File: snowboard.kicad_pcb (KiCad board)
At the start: 4 copper layers, 80 x 104.5 mm, 6 parts, among them J1 AMPHENOL_10118193-0001LF, SW1 BOOT, SW2 RESET, U1 XCVR_ESP32-WROVER-E-N4R8, U2 IC_CP2102N-A02-GQFN28R

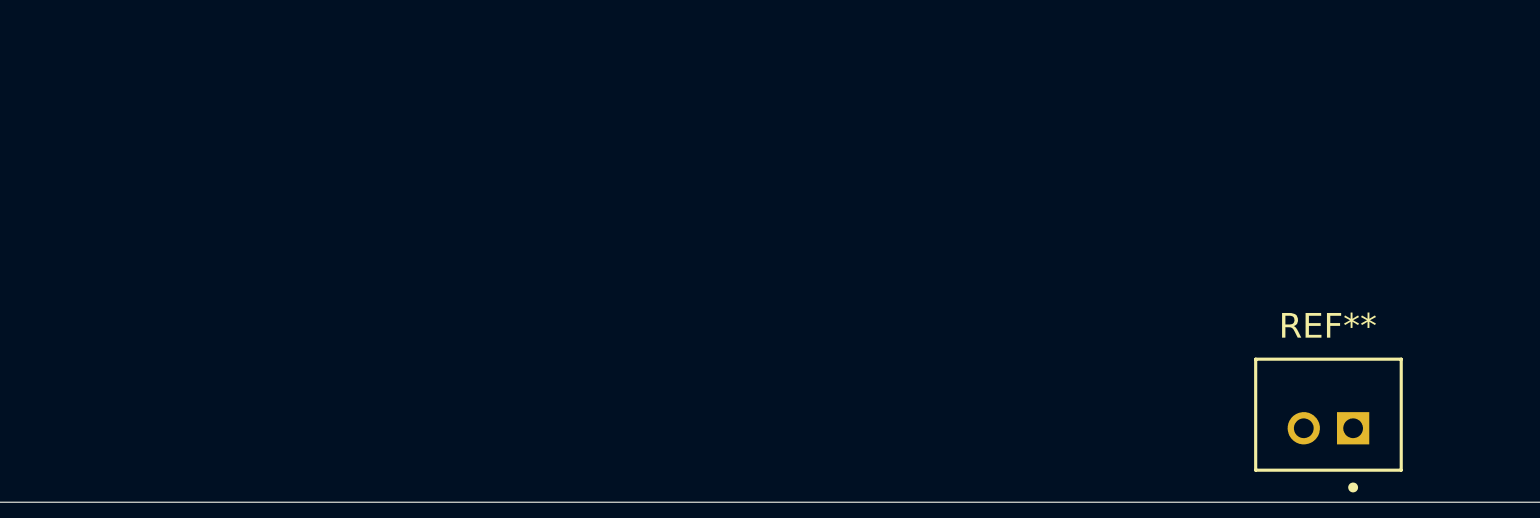
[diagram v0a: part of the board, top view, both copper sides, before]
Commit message: Update battery connector
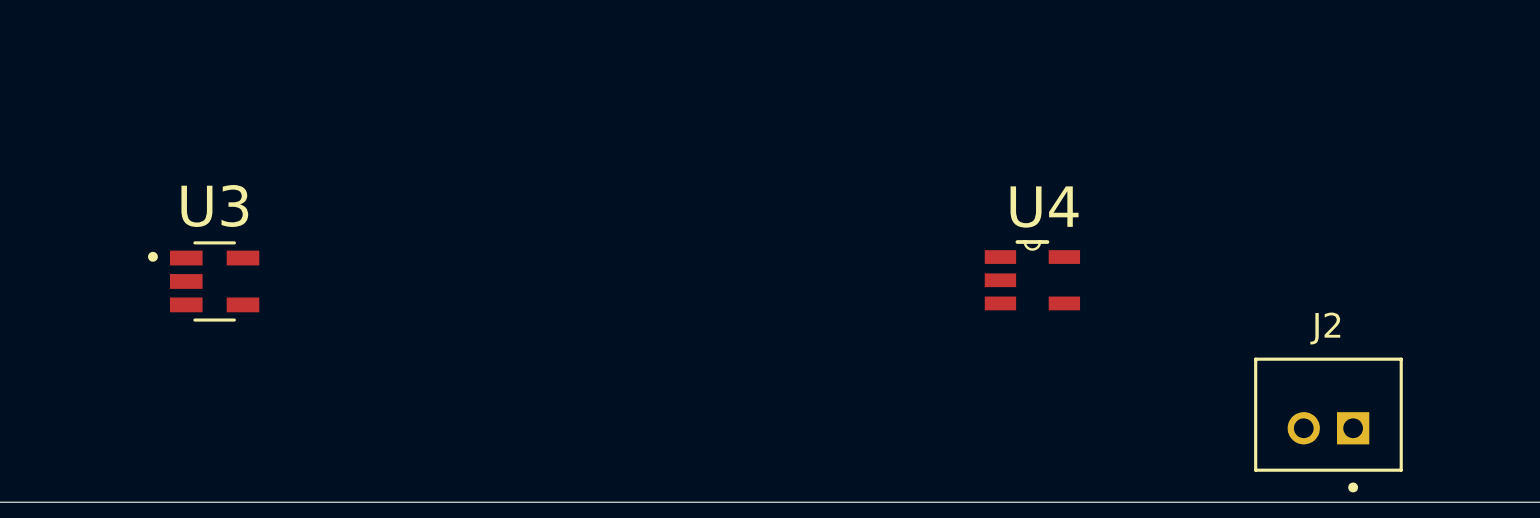
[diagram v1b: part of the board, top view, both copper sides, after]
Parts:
- added U3: SOT95P280X145-5N, USER_FP:SOT95P280X145-5N, F.Cu at (127.8, 146.1)
- added U4: SOT95P280X145-5N, USER_FP:MCP73831T-2ACI, F.Cu at (161.0, 146.0)
- renumbered REF** to J2

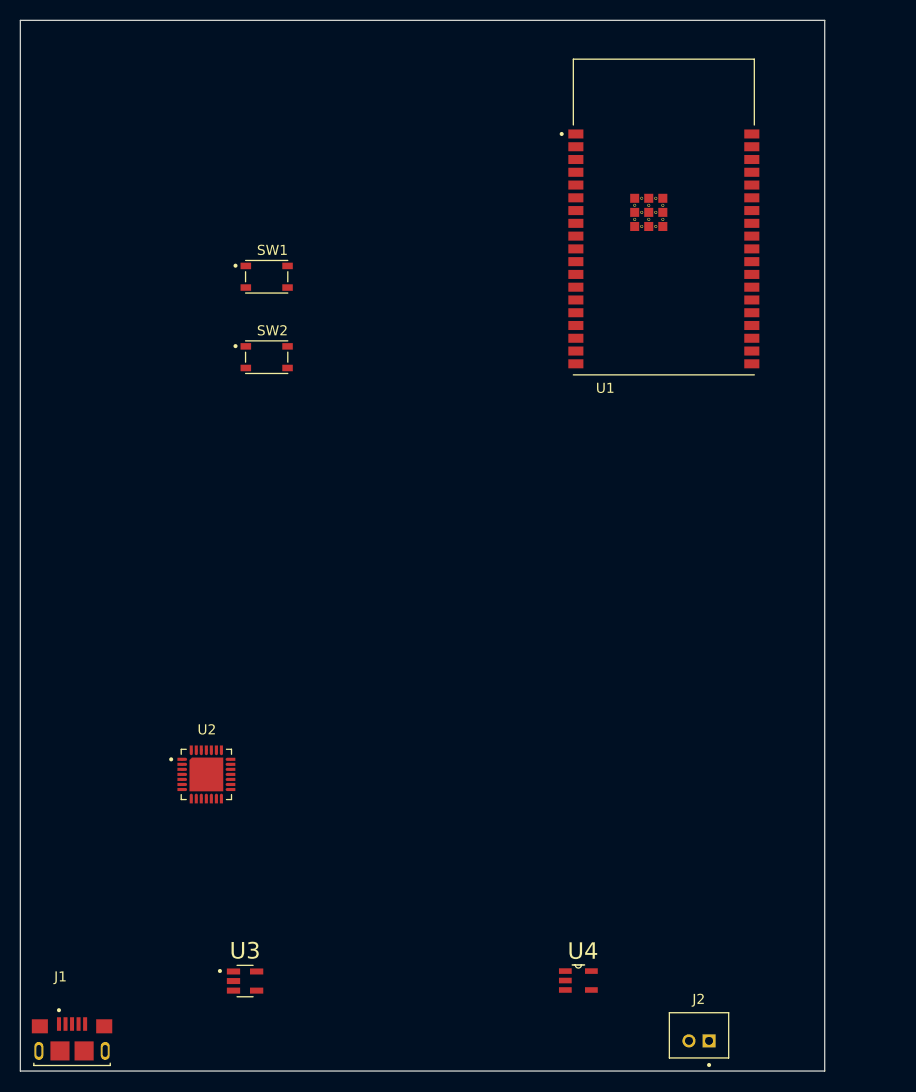
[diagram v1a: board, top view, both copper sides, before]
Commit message: Add footprints and models and place components on PCB
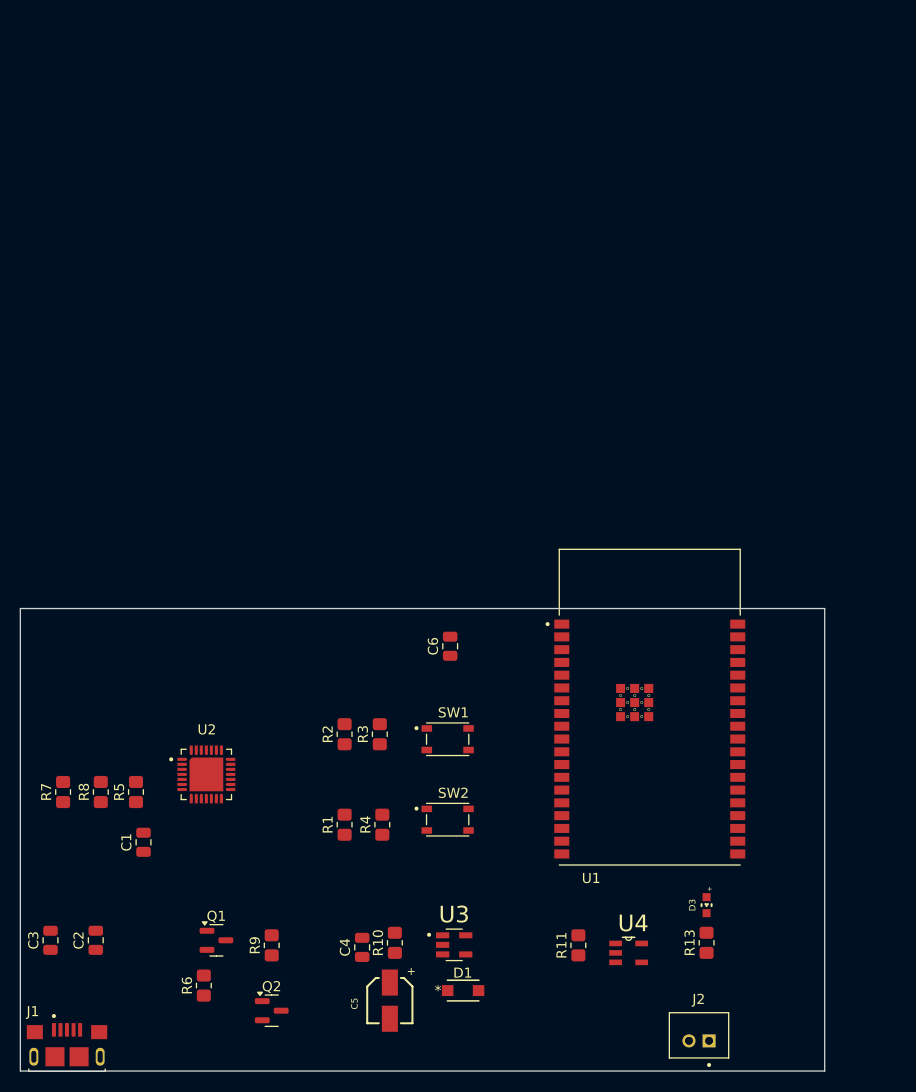
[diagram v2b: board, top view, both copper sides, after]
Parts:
- added C1: 1uF, Capacitor_SMD:C_0805_2012Metric, F.Cu at (117.8, 132.2)
- added C2: 10uF, Capacitor_SMD:C_0805_2012Metric, F.Cu at (113.0, 142.0)
- added C3: 100nF, Capacitor_SMD:C_0805_2012Metric, F.Cu at (108.5, 142.0)
- added C4: 10uF, Capacitor_SMD:C_0805_2012Metric, F.Cu at (139.5, 142.7)
- added C5: 1uF, USER_FP:WCAP-ASLL_4X5.5_DXL_, F.Cu at (142.2, 148.0)
- added C6: 10uF, Capacitor_SMD:C_0805_2012Metric, F.Cu at (148.2, 112.8)
- added D1: MBR120, USER_FP:MBR120_SDO_SOD-123FL498_OSI, F.Cu at (149.5, 147.0)
- added D3: Charge Status, USER_FP:WL-SMCW_0603, F.Cu at (173.8, 138.5)
- added Q1: S8050, Package_TO_SOT_SMD:SOT-23, F.Cu at (125.0, 142.0)
- added Q2: S8050, Package_TO_SOT_SMD:SOT-23, F.Cu at (130.5, 149.0)
- added R1: 10k, Resistor_SMD:R_0805_2012Metric_Pad1.20x1.40mm_HandSolder, F.Cu at (137.8, 130.5)
- added R10: 100K, Resistor_SMD:R_0805_2012Metric_Pad1.20x1.40mm_HandSolder, F.Cu at (142.8, 142.2)
- added R11: 5k, Resistor_SMD:R_0805_2012Metric_Pad1.20x1.40mm_HandSolder, F.Cu at (161.0, 142.5)
- added R13: 1k, Resistor_SMD:R_0805_2012Metric_Pad1.20x1.40mm_HandSolder, F.Cu at (173.8, 142.2)
- added R2: 10k, Resistor_SMD:R_0805_2012Metric_Pad1.20x1.40mm_HandSolder, F.Cu at (137.8, 121.5)
- added R3: 470, Resistor_SMD:R_0805_2012Metric_Pad1.20x1.40mm_HandSolder, F.Cu at (141.2, 121.5)
- added R4: 470, Resistor_SMD:R_0805_2012Metric_Pad1.20x1.40mm_HandSolder, F.Cu at (141.5, 130.5)
- added R5: 470, Resistor_SMD:R_0805_2012Metric_Pad1.20x1.40mm_HandSolder, F.Cu at (117.0, 127.2)
- added R6: 12k, Resistor_SMD:R_0805_2012Metric_Pad1.20x1.40mm_HandSolder, F.Cu at (123.8, 146.5)
- added R7: 47.5K, Resistor_SMD:R_0805_2012Metric_Pad1.20x1.40mm_HandSolder, F.Cu at (109.8, 127.2)
- added R8: 22.1K, Resistor_SMD:R_0805_2012Metric_Pad1.20x1.40mm_HandSolder, F.Cu at (113.5, 127.2)
- added R9: 12k, Resistor_SMD:R_0805_2012Metric_Pad1.20x1.40mm_HandSolder, F.Cu at (130.5, 142.5)
- J1: value AMPHENOL_10118193-0001LF -> Micro USB Port
- J2: value JST_B2B-PH-K-S -> B2B-PH-K-S
- U1: value XCVR_ESP32-WROVER-E-N4R8 -> ESP32-WROVER-E-N4R8
- U2: value IC_CP2102N-A02-GQFN28R -> CP2102N-A02-GQFN28R
- U3: value SOT95P280X145-5N -> SPX3819M5-L-3-3
- U4: value SOT95P280X145-5N -> MCP73831T-2ACI_OT
- moved SW1 49.4 mm to (148.0, 122.0)
- moved SW2 49.4 mm to (148.0, 130.0)
- moved U1 48.8 mm to (168.1, 118.8)
- moved U3 21.1 mm to (148.7, 142.4)
- moved U4 5.71 mm to (166.0, 143.2)
- moved J1 0.77 mm to (110.1, 153.6)
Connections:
- J1 pad 1: (no net) -> VBUS
- J1 pad 2: (no net) -> /D_N
- J1 pad 3: (no net) -> /D_P
- J1 pad 4: (no net) -> unconnected-(J1-ID-Pad4)
- J1 pad 5: (no net) -> GND
- J1 pad S1: (no net) -> unconnected-(J1-SHIELD-PadS1)
- J1 pad S2: (no net) -> unconnected-(J1-SHIELD__1-PadS2)
- J1 pad S3: (no net) -> unconnected-(J1-SHIELD__2-PadS3)
- J1 pad S4: (no net) -> unconnected-(J1-SHIELD__3-PadS4)
- J1 pad S5: (no net) -> unconnected-(J1-SHIELD__4-PadS5)
- J1 pad S6: (no net) -> unconnected-(J1-SHIELD__5-PadS6)
- J2 pad 1: (no net) -> +BATT
- J2 pad 2: (no net) -> GND
- SW1 pad 1: (no net) -> Net-(R3-Pad1)
- SW1 pad 2: (no net) -> unconnected-(SW1-Pad2)
- SW1 pad 3: (no net) -> unconnected-(SW1-Pad3)
- SW1 pad 4: (no net) -> /IO0
- SW2 pad 1: (no net) -> Net-(R4-Pad1)
- SW2 pad 2: (no net) -> unconnected-(SW2-Pad2)
- SW2 pad 3: (no net) -> unconnected-(SW2-Pad3)
- SW2 pad 4: (no net) -> /AEN
- U1 pad 1: (no net) -> GND
- U1 pad 10: (no net) -> unconnected-(U1-IO25-Pad10)
- U1 pad 11: (no net) -> unconnected-(U1-IO26-Pad11)
- U1 pad 12: (no net) -> unconnected-(U1-IO27-Pad12)
- U1 pad 13: (no net) -> unconnected-(U1-IO14-Pad13)
- U1 pad 14: (no net) -> unconnected-(U1-IO12-Pad14)
- U1 pad 15: (no net) -> GND
- U1 pad 16: (no net) -> unconnected-(U1-IO13-Pad16)
- U1 pad 17: (no net) -> unconnected-(U1-NC-Pad17)
- U1 pad 18: (no net) -> unconnected-(U1-NC__1-Pad18)
- U1 pad 19: (no net) -> unconnected-(U1-NC__2-Pad19)
- U1 pad 2: (no net) -> +3.3V
- U1 pad 20: (no net) -> unconnected-(U1-NC__3-Pad20)
- U1 pad 21: (no net) -> unconnected-(U1-NC__4-Pad21)
- U1 pad 22: (no net) -> unconnected-(U1-NC__5-Pad22)
- U1 pad 23: (no net) -> unconnected-(U1-IO15-Pad23)
- U1 pad 24: (no net) -> unconnected-(U1-IO2-Pad24)
- U1 pad 25: (no net) -> /IO0
- U1 pad 26: (no net) -> unconnected-(U1-IO4-Pad26)
- U1 pad 27: (no net) -> unconnected-(U1-NC__6-Pad27)
- U1 pad 28: (no net) -> unconnected-(U1-NC__7-Pad28)
- U1 pad 29: (no net) -> unconnected-(U1-IO5-Pad29)
- U1 pad 3: (no net) -> /AEN
- U1 pad 30: (no net) -> unconnected-(U1-IO18-Pad30)
- U1 pad 31: (no net) -> unconnected-(U1-IO19-Pad31)
- U1 pad 32: (no net) -> unconnected-(U1-NC__8-Pad32)
- U1 pad 33: (no net) -> unconnected-(U1-IO21-Pad33)
- U1 pad 34: (no net) -> /RX
- U1 pad 35: (no net) -> /TX
- U1 pad 36: (no net) -> unconnected-(U1-IO22-Pad36)
- U1 pad 37: (no net) -> unconnected-(U1-IO23-Pad37)
- U1 pad 38: (no net) -> GND
- U1 pad 39_1: (no net) -> unconnected-(U1-EXP-Pad39_1)
- U1 pad 39_2: (no net) -> unconnected-(U1-EXP__1-Pad39_2)
- U1 pad 39_3: (no net) -> unconnected-(U1-EXP__2-Pad39_3)
- U1 pad 39_4: (no net) -> unconnected-(U1-EXP__3-Pad39_4)
- U1 pad 39_5: (no net) -> unconnected-(U1-EXP__4-Pad39_5)
- U1 pad 39_6: (no net) -> unconnected-(U1-EXP__5-Pad39_6)
- U1 pad 39_7: (no net) -> unconnected-(U1-EXP__6-Pad39_7)
- U1 pad 39_8: (no net) -> unconnected-(U1-EXP__7-Pad39_8)
- U1 pad 39_9: (no net) -> unconnected-(U1-EXP__8-Pad39_9)
- U1 pad 4: (no net) -> unconnected-(U1-SENSOR_VP-Pad4)
- U1 pad 5: (no net) -> unconnected-(U1-SENSOR_VN-Pad5)
- U1 pad 6: (no net) -> unconnected-(U1-IO34-Pad6)
- U1 pad 7: (no net) -> unconnected-(U1-IO35-Pad7)
- U1 pad 8: (no net) -> unconnected-(U1-IO32-Pad8)
- U1 pad 9: (no net) -> unconnected-(U1-IO33-Pad9)
- U2 pad 1: (no net) -> unconnected-(U2-DCD-Pad1)
- U2 pad 10: (no net) -> unconnected-(U2-NC-Pad10)
- U2 pad 11: (no net) -> unconnected-(U2-~{SUSPEND}-Pad11)
- U2 pad 12: (no net) -> unconnected-(U2-SUSPEND-Pad12)
- U2 pad 13: (no net) -> unconnected-(U2-CHREN-Pad13)
- U2 pad 14: (no net) -> unconnected-(U2-CHR1-Pad14)
- U2 pad 15: (no net) -> unconnected-(U2-CHR0-Pad15)
- U2 pad 16: (no net) -> unconnected-(U2-GPIO3_WAKEUP-Pad16)
- U2 pad 17: (no net) -> unconnected-(U2-GPIO2_RS485-Pad17)
- U2 pad 18: (no net) -> unconnected-(U2-GPIO1_RXT-Pad18)
- U2 pad 19: (no net) -> unconnected-(U2-GPIO0_TXT-Pad19)
- U2 pad 2: (no net) -> unconnected-(U2-RI/CLK-Pad2)
- U2 pad 20: (no net) -> unconnected-(U2-GPIO6-Pad20)
- U2 pad 21: (no net) -> unconnected-(U2-GPIO5-Pad21)
- U2 pad 22: (no net) -> unconnected-(U2-GPIO4-Pad22)
- U2 pad 23: (no net) -> unconnected-(U2-CTS-Pad23)
- U2 pad 24: (no net) -> /RTS
- U2 pad 25: (no net) -> /TX
- U2 pad 26: (no net) -> Net-(U2-TXD)
- U2 pad 27: (no net) -> unconnected-(U2-DSR-Pad27)
- U2 pad 28: (no net) -> /DTR
- U2 pad 29: (no net) -> GND
- U2 pad 3: (no net) -> GND
- U2 pad 4: (no net) -> /D_P
- U2 pad 5: (no net) -> /D_N
- U2 pad 6: (no net) -> Net-(U2-VDD)
- U2 pad 7: (no net) -> VBUS
- U2 pad 8: (no net) -> Net-(U2-VBUS)
- U2 pad 9: (no net) -> unconnected-(U2-~{RST}-Pad9)
- U3 pad 1: (no net) -> VBUS
- U3 pad 2: (no net) -> GND
- U3 pad 3: (no net) -> Net-(U3-EN)
- U3 pad 4: (no net) -> GND
- U3 pad 5: (no net) -> +3.3V
- U4 pad 1: (no net) -> Net-(U4-STAT)
- U4 pad 2: (no net) -> GND
- U4 pad 3: (no net) -> +BATT
- U4 pad 4: (no net) -> VBUS
- U4 pad 5: (no net) -> Net-(U4-PROG)
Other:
- board size 80 x 104.5 mm -> 80 x 46 mm

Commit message: PCB routing mostly done
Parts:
- moved J1 78.6 mm to (184.2, 127.2), turned to 90 degrees
- moved R7 74.5 mm to (183.8, 118.5), turned to -90 degrees
- moved C3 69.2 mm to (175.8, 125.8)
- moved R8 68.8 mm to (181.8, 118.5)
- moved C1 65.9 mm to (182.8, 121.5), turned to 0 degrees
- moved C2 62.9 mm to (173.8, 125.8)
- moved R6 56.1 mm to (168.0, 112.0), turned to 0 degrees
- moved Q1 55.1 mm to (171.8, 113.0), turned to 180 degrees
- moved R5 53.7 mm to (170.0, 118.8), turned to 0 degrees
- moved U2 53.6 mm to (177.0, 117.5), turned to 90 degrees
- moved Q2 50.6 mm to (168.0, 115.0), turned to 90 degrees
- moved R9 49.1 mm to (171.8, 115.8), turned to 0 degrees
- moved D1 32.9 mm to (180.2, 135.2), turned to -90 degrees
- moved C4 31.8 mm to (170.2, 134.8)
- moved R10 30.7 mm to (172.2, 133.8)
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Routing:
- net /AEN: track 0.00 -> 51.7 mm, vias 0 -> 3
- net GND: track 0.00 -> 48.8 mm, vias 0 -> 8
- net +3.3V: track 0.00 -> 38.6 mm, vias 0 -> 3
- net /IO0: track 0.00 -> 24.6 mm, vias 0 -> 2
- net VBUS: track 0.00 -> 23.9 mm, vias 0 -> 4
- net /TX: track 0.00 -> 21.3 mm
- net /RX: track 0.00 -> 15.7 mm
- net /DTR: track 0.00 -> 12.7 mm, vias 0 -> 2
- net /D_P: track 0.00 -> 11.3 mm
- net /D_N: track 0.00 -> 11.0 mm, vias 0 -> 2
- net +BATT: track 0.00 -> 6.60 mm
- net Net-(U4-STAT): track 0.00 -> 5.43 mm
- net Net-(U3-EN): track 0.00 -> 5.08 mm
- net Net-(U2-VBUS): track 0.00 -> 4.97 mm
- net Net-(U2-VDD): track 0.00 -> 4.80 mm
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- added copper zone on In2.Cu, net +3.3V
- added copper zone on In1.Cu, net GND
- added copper zone on In2.Cu, net VBUS
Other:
- board size 80 x 46 mm -> 51.8 x 35.5 mm

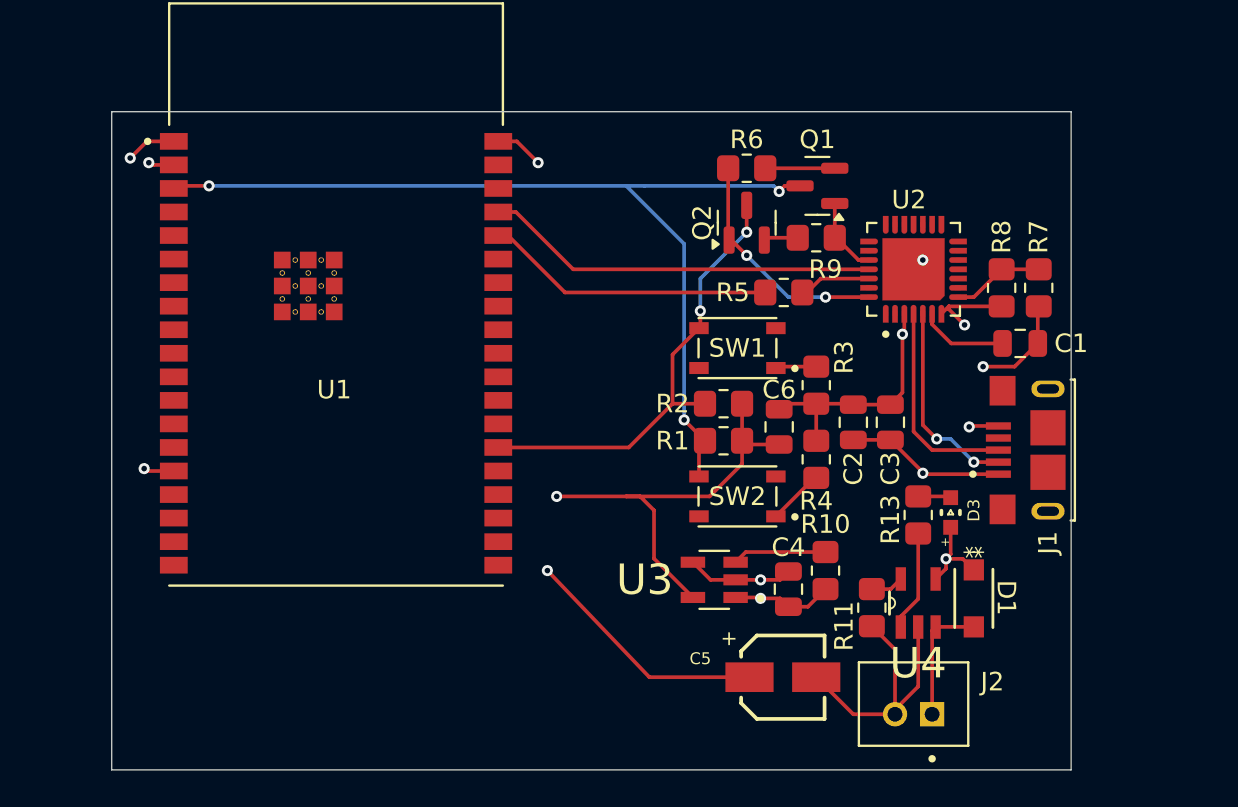
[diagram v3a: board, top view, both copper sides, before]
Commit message: Add IMU
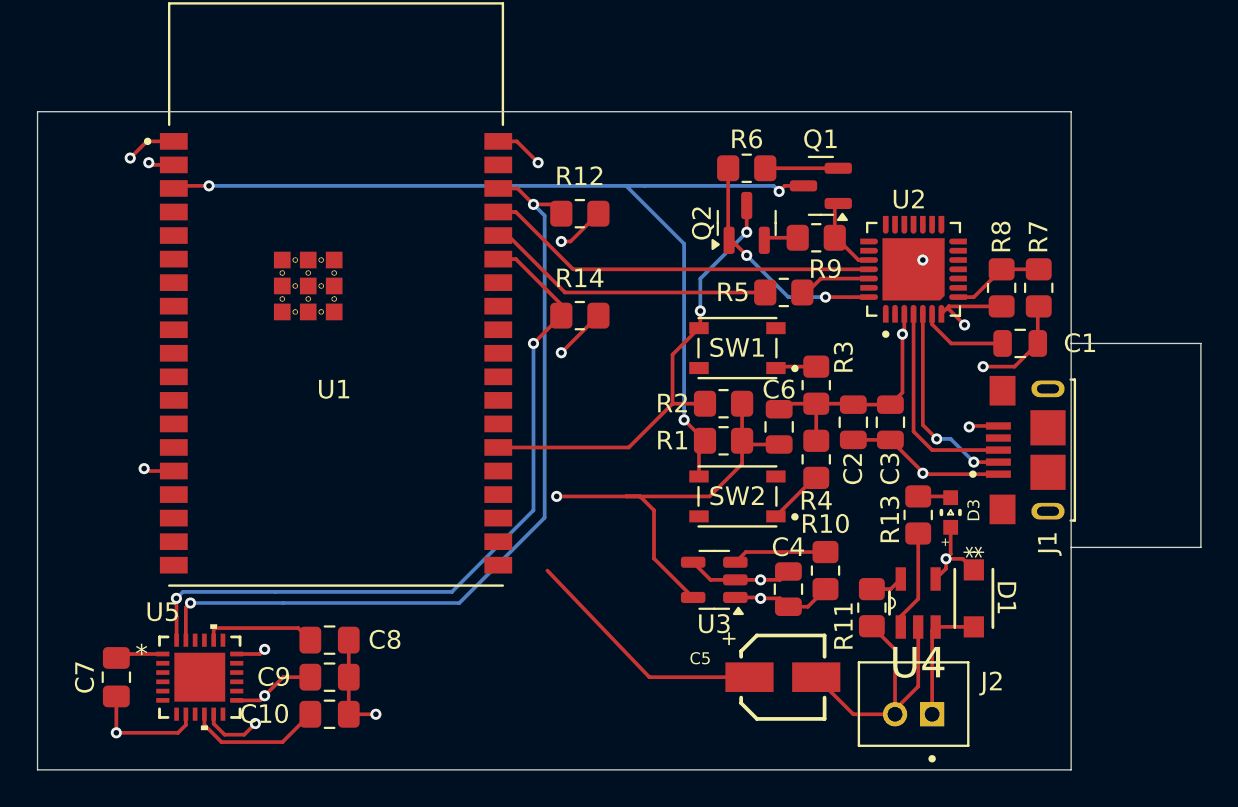
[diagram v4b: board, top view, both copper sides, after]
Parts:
- added C10: 0.1uF, Capacitor_SMD:C_0805_2012Metric_Pad1.18x1.45mm_HandSolder, F.Cu at (145.5, 141.5)
- added C7: 0.1uF, Capacitor_SMD:C_0805_2012Metric_Pad1.18x1.45mm_HandSolder, F.Cu at (134.0, 139.5)
- added C8: 2.2nF, Capacitor_SMD:C_0805_2012Metric_Pad1.18x1.45mm_HandSolder, F.Cu at (145.5, 137.5)
- added C9: 10nF, Capacitor_SMD:C_0805_2012Metric_Pad1.18x1.45mm_HandSolder, F.Cu at (145.5, 139.5)
- added R12: 100k, Resistor_SMD:R_0805_2012Metric_Pad1.20x1.40mm_HandSolder, F.Cu at (159.0, 114.5)
- added R14: 100k, Resistor_SMD:R_0805_2012Metric_Pad1.20x1.40mm_HandSolder, F.Cu at (159.0, 120.0)
- added U5: MPU-6050, USER_FP:MPU6050_QFN24_4X4X0P9-0P5_TDK, F.Cu at (138.5, 139.5)
- U3: footprint USER_FP:SOT95P280X145-5N -> Package_TO_SOT_SMD:SOT-23-5
- moved Q1 0.19 mm to (172.0, 113.0)
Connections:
- U1 pad 33: unconnected-(U1-IO21-Pad33) -> /I2C_SDA
- U1 pad 36: unconnected-(U1-IO22-Pad36) -> /I2C_SCL
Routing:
- net /I2C_SCL: track 0.00 -> 44.2 mm, vias 0 -> 2
- net /I2C_SDA: track 0.00 -> 39.6 mm, vias 0 -> 2
- net +3.3V: track 38.6 -> 55.0 mm, vias 3 -> 6
- net GND: track 48.8 -> 61.2 mm, vias 8 -> 11
- net Net-(U5-REGOUT): track 0.00 -> 7.30 mm
- net Net-(U5-CPOUT): track 0.00 -> 6.09 mm
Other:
- board size 51.8 x 35.5 mm -> 62.8 x 35.5 mm
